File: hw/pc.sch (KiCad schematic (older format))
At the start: 10 parts

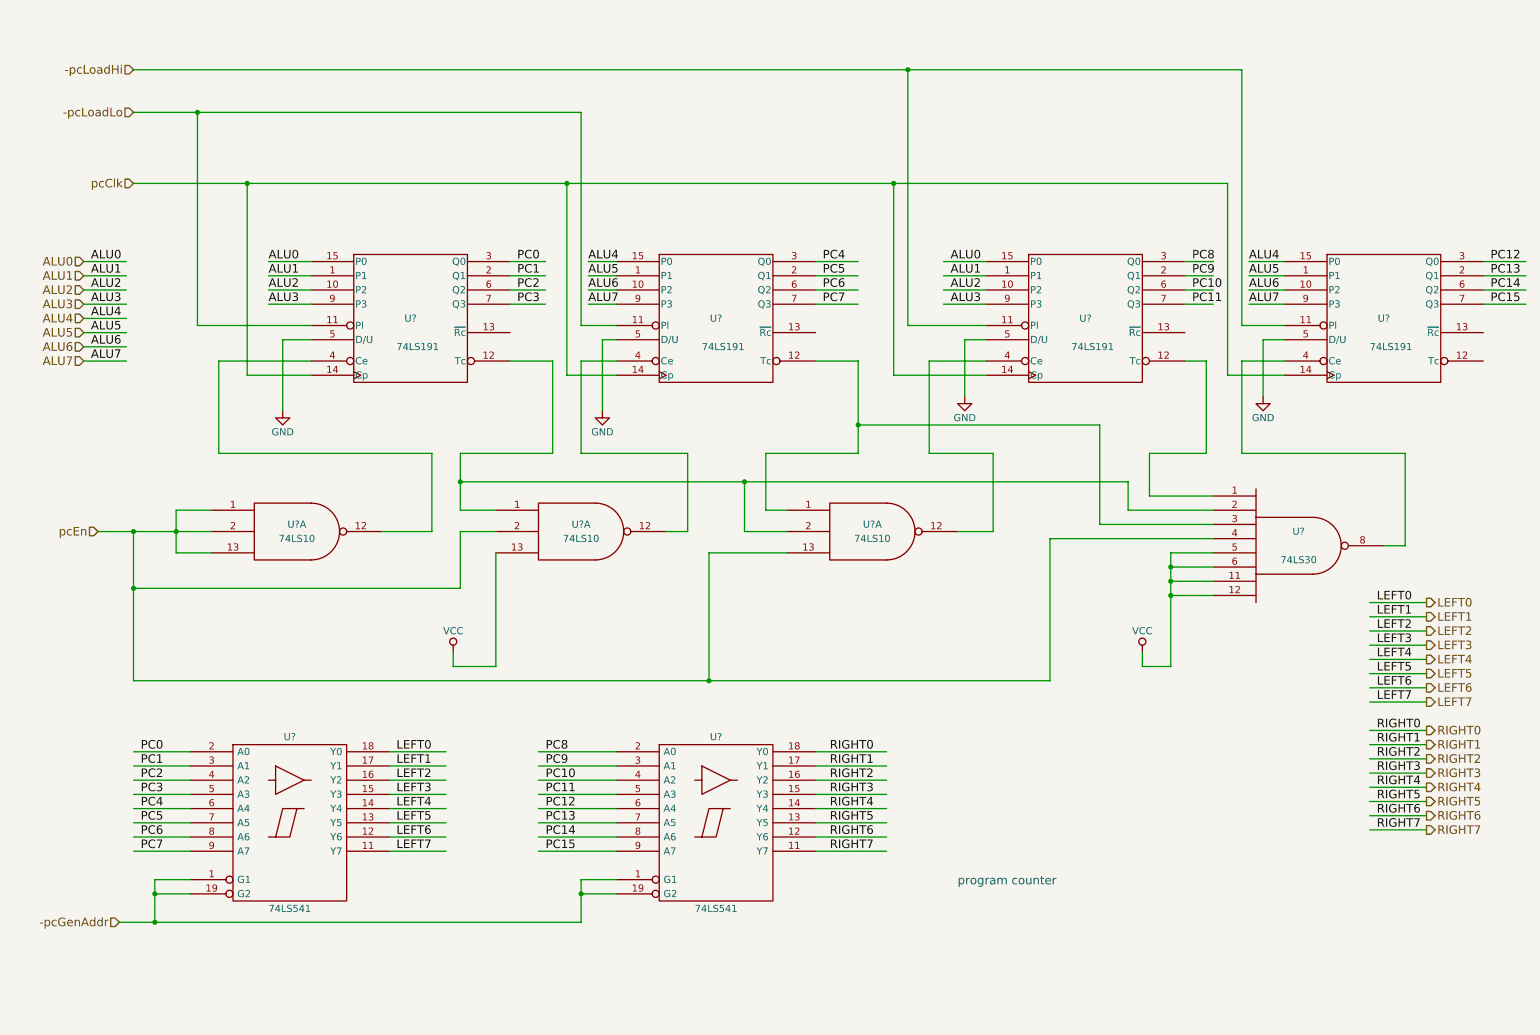
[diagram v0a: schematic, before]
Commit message: annotated more components
Also some more work on connecting modules together
and adding glue logic.
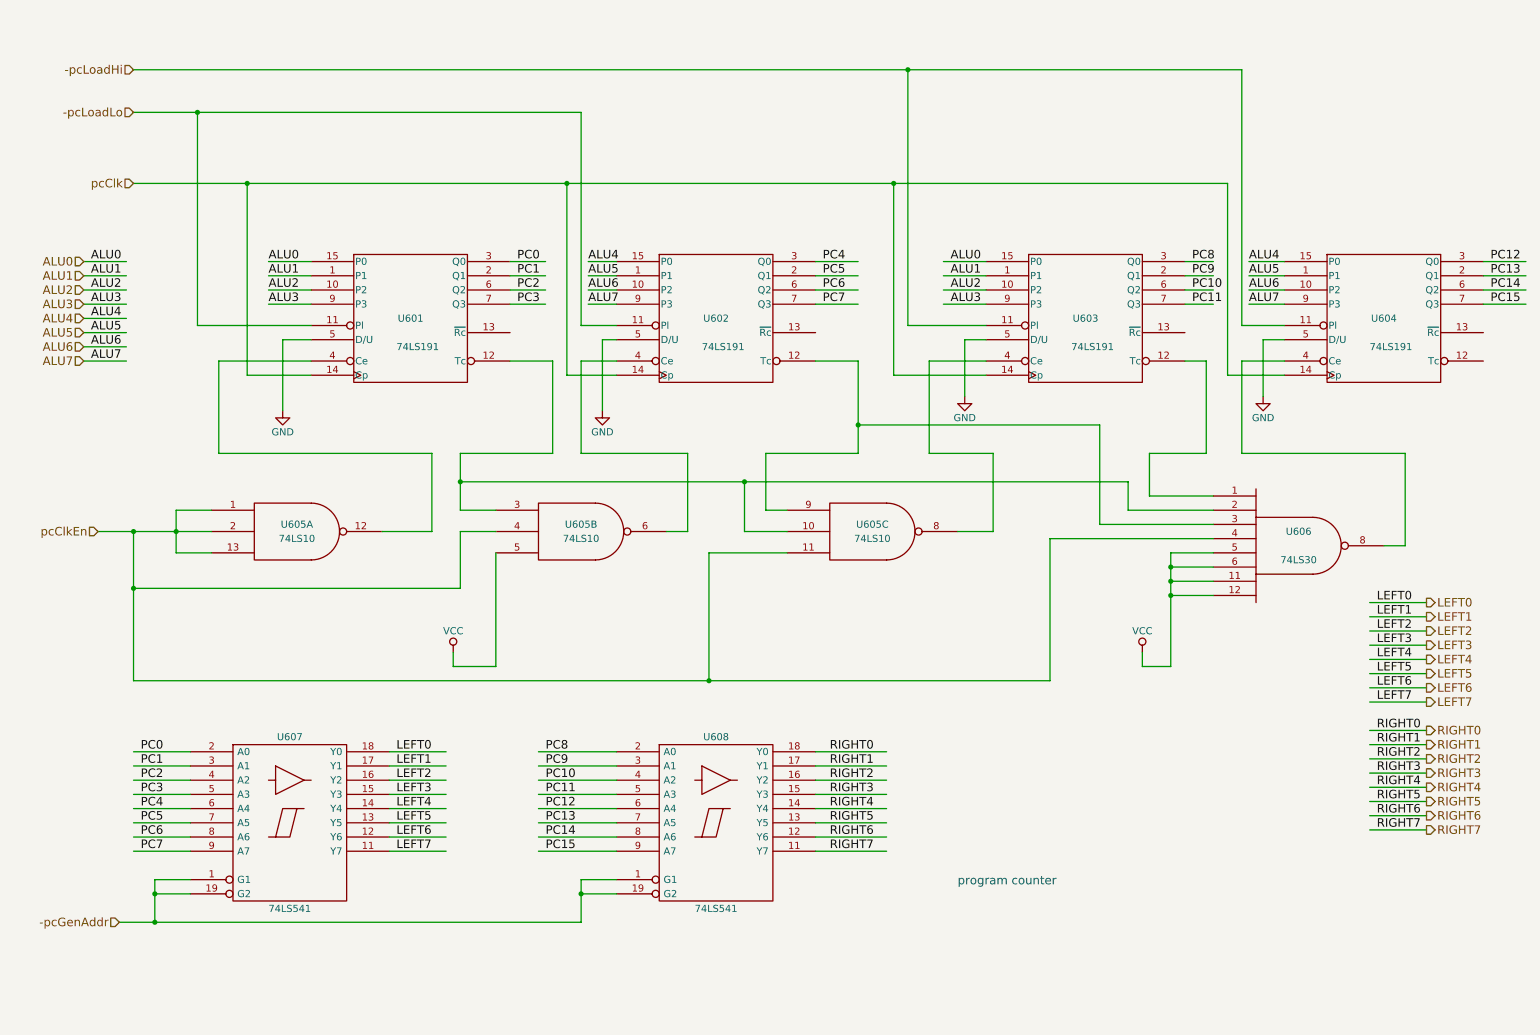
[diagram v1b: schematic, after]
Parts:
- gave numbers to parts that had none: 8
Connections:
- net labels added: pcClkEn
- net labels removed: pcEn
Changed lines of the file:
@@
 $EndDescr
 $Comp
-L 74LS10 U?
+L 74LS10 U605
 U 1 1 592B9492
 P 2500 4250
-F 0 "U?" H 2500 4300 50  0000 C CNN
+F 0 "U605" H 2500 4300 50  0000 C CNN
 F 1 "74LS10" H 2500 4200 50  0000 C CNN
 F 2 "" H 2500 4250 50  0001 C CNN
@@
 $EndComp
 $Comp
-L 74LS30 U?
+L 74LS30 U606
 U 1 1 592B9499
 P 9550 4350
-F 0 "U?" H 9550 4450 50  0000 C CNN
+F 0 "U606" H 9550 4450 50  0000 C CNN
 F 1 "74LS30" H 9550 4250 50  0000 C CNN
 F 2 "" H 9550 4350 50  0001 C CNN
@@
 $EndComp
 $Comp
-L 74LS191 U?
+L 74LS191 U601
 U 1 1 592B94A0
 P 3300 2750
-F 0 "U?" H 3300 2750 50  0000 C CNN
+F 0 "U601" H 3300 2750 50  0000 C CNN
 F 1 "74LS191" H 3350 2550 50  0000 C CNN
 F 2 "" H 3300 2750 50  0001 C CNN
@@
 $EndComp
 $Comp
-L 74LS191 U?
+L 74LS191 U602
 U 1 1 592B94A7
 P 5450 2750
-F 0 "U?" H 5450 2750 50  0000 C CNN
+F 0 "U602" H 5450 2750 50  0000 C CNN
 F 1 "74LS191" H 5500 2550 50  0000 C CNN
 F 2 "" H 5450 2750 50  0001 C CNN
@@
 $EndComp
 $Comp
-L 74LS191 U?
+L 74LS191 U603
 U 1 1 592B94AE
 P 8050 2750
-F 0 "U?" H 8050 2750 50  0000 C CNN
+F 0 "U603" H 8050 2750 50  0000 C CNN
 F 1 "74LS191" H 8100 2550 50  0000 C CNN
 F 2 "" H 8050 2750 50  0001 C CNN
@@
 $EndComp
 $Comp
-L 74LS191 U?
+L 74LS191 U604
 U 1 1 592B94B5
 P 10150 2750
-F 0 "U?" H 10150 2750 50  0000 C CNN
+F 0 "U604" H 10150 2750 50  0000 C CNN
 F 1 "74LS191" H 10200 2550 50  0000 C CNN
 F 2 "" H 10150 2750 50  0001 C CNN
@@
 $EndComp
 $Comp
-L 74LS10 U?
-U 1 1 592B94BC
+L 74LS10 U605
+U 2 1 592B94BC
 P 4500 4250
-F 0 "U?" H 4500 4300 50  0000 C CNN
+F 0 "U605" H 4500 4300 50  0000 C CNN
 F 1 "74LS10" H 4500 4200 50  0000 C CNN
 F 2 "" H 4500 4250 50  0001 C CNN
 F 3 "" H 4500 4250 50  0001 C CNN
-	1    4500 4250
-	1    0    0    -1
-$EndComp
-$Comp
-L 74LS10 U?
-U 1 1 592B94C3
+	2    4500 4250
+	1    0    0    -1
+$EndComp
+$Comp
+L 74LS10 U605
+U 3 1 592B94C3
 P 6550 4250
-F 0 "U?" H 6550 4300 50  0000 C CNN
+F 0 "U605" H 6550 4300 50  0000 C CNN
 F 1 "74LS10" H 6550 4200 50  0000 C CNN
 F 2 "" H 6550 4250 50  0001 C CNN
 F 3 "" H 6550 4250 50  0001 C CNN
-	1    6550 4250
+	3    6550 4250
 	1    0    0    -1
 $EndComp
@@
 $EndComp
 $Comp
-L 74LS541 U?
+L 74LS541 U607
 U 1 1 592B94F7
 P 2450 6300
-F 0 "U?" H 2450 6875 50  0000 C BNN
+F 0 "U607" H 2450 6875 50  0000 C BNN
 F 1 "74LS541" H 2450 5725 50  0000 C TNN
 F 2 "" H 2450 6300 50  0001 C CNN
@@
 $EndComp
 $Comp
-L 74LS541 U?
+L 74LS541 U608
 U 1 1 592B94FE
 P 5450 6300
-F 0 "U?" H 5450 6875 50  0000 C BNN
+F 0 "U608" H 5450 6875 50  0000 C BNN
 F 1 "74LS541" H 5450 5725 50  0000 C TNN
 F 2 "" H 5450 6300 50  0001 C CNN
@@
 pcClk
 Text HLabel 1100 4250 0    60   Input ~ 0
-pcEn
+pcClkEn
 Text HLabel 1250 7000 0    60   Input ~ 0
 -pcGenAddr

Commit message: eliminated pcClkEn signal
There's no need to selectively enable/disable
the count function in the PC because the PC
clock signal (pcClk) is generated explicitly
by the microcode, and clock pulses are sent
only when we actually want to increment the PC
value.

This allowed a simplicification of the carry
logic, and eliminated the need for the 74HC30
in the last stage of the carry logic.
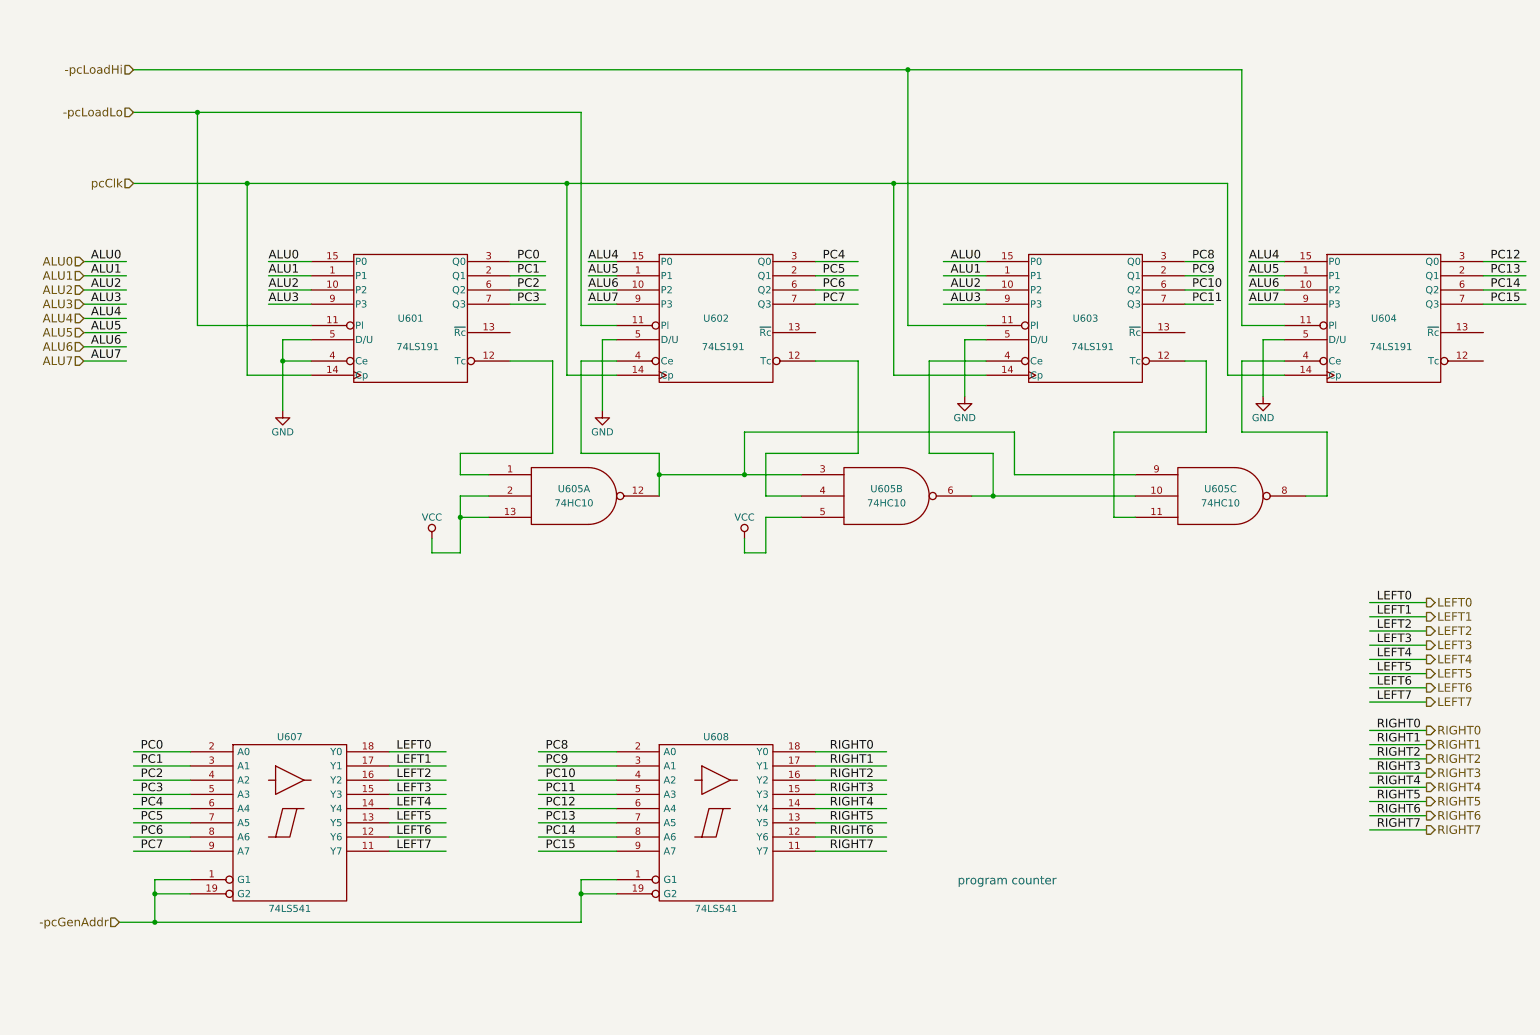
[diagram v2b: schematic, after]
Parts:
- removed U606: 74LS30, symbol 74LS30
- U605: value 74LS10 -> 74HC10
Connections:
- net labels removed: pcClkEn
- wire segments 188 -> 179

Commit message: fix PC carry logic
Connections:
- wire segments 179 -> 169
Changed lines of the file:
@@
 L GND #PWR?
 U 1 1 592B94E2
-P 4650 3400
-F 0 "#PWR?" H 4650 3150 50  0001 C CNN
-F 1 "GND" H 4650 3250 50  0000 C CNN
-F 2 "" H 4650 3400 50  0001 C CNN
-F 3 "" H 4650 3400 50  0001 C CNN
-	1    4650 3400
+P 4650 3250
+F 0 "#PWR?" H 4650 3000 50  0001 C CNN
+F 1 "GND" H 4650 3100 50  0000 C CNN
+F 2 "" H 4650 3250 50  0001 C CNN
+F 3 "" H 4650 3250 50  0001 C CNN
+	1    4650 3250
 	1    0    0    -1
 $EndComp
@@
 L GND #PWR?
 U 1 1 592B94E8
-P 7200 3300
-F 0 "#PWR?" H 7200 3050 50  0001 C CNN
-F 1 "GND" H 7200 3150 50  0000 C CNN
-F 2 "" H 7200 3300 50  0001 C CNN
-F 3 "" H 7200 3300 50  0001 C CNN
-	1    7200 3300
+P 7200 3200
+F 0 "#PWR?" H 7200 2950 50  0001 C CNN
+F 1 "GND" H 7200 3050 50  0000 C CNN
+F 2 "" H 7200 3200 50  0001 C CNN
+F 3 "" H 7200 3200 50  0001 C CNN
+	1    7200 3200
 	1    0    0    -1
 $EndComp
@@
 	2600 2900 2400 2900
 Wire Wire Line
-	2400 2900 2400 3050
-Wire Wire Line
-	2400 3050 2400 3400
+	2400 2900 2400 3400
 Wire Wire Line
 	4750 2900 4650 2900
 Wire Wire Line
-	4650 2900 4650 3400
+	4650 2900 4650 3250
 Wire Wire Line
 	7350 2900 7200 2900
 Wire Wire Line
-	7200 2900 7200 3300
+	7200 2900 7200 3200
 Wire Wire Line
 	9450 2900 9300 2900
@@
 	9450 3150 9050 3150
 Wire Wire Line
-	9050 3150 9050 1800
-Wire Wire Line
-	9050 1800 6700 1800
-Wire Wire Line
-	6700 1800 4400 1800
-Wire Wire Line
-	4400 1800 2150 1800
-Wire Wire Line
-	2150 1800 1350 1800
+	9050 1800 9050 3150
+Wire Wire Line
+	1350 1800 9050 1800
 Wire Wire Line
 	7350 3150 6700 3150
@@
 	1800 2800 1800 1300
 Wire Wire Line
-	1350 1300 1800 1300
-Wire Wire Line
-	1800 1300 4500 1300
+	1350 1300 4500 1300
 Wire Wire Line
 	4750 2800 4500 2800
@@
 	6800 2800 6800 1000
 Wire Wire Line
-	1350 1000 6800 1000
-Wire Wire Line
-	6800 1000 9150 1000
+	1350 1000 9150 1000
 Wire Wire Line
 	9450 2800 9150 2800
@@
 	1750 6700 1500 6700
 Wire Wire Line
-	1500 6700 1500 6800
-Wire Wire Line
-	1500 6800 1500 7000
+	1500 6700 1500 7000
 Wire Wire Line
 	1750 6800 1500 6800
 Connection ~ 1500 6800
 Wire Wire Line
-	4500 7000 1500 7000
-Wire Wire Line
-	1500 7000 1250 7000
+	4500 7000 1250 7000
 Wire Wire Line
 	4750 6700 4500 6700
 Wire Wire Line
-	4500 6700 4500 6800
-Wire Wire Line
-	4500 6800 4500 7000
+	4500 6700 4500 7000
 Connection ~ 1500 7000
 Wire Wire Line
@@
 	4300 3700 3650 3700
 Wire Wire Line
-	5050 4000 5050 3850
-Wire Wire Line
-	5050 3850 5050 3700
+	5050 3700 5050 4000
 Wire Wire Line
 	5050 3700 4500 3700
@@
 	4500 3700 4500 3050
 Wire Wire Line
-	6050 3850 5650 3850
-Wire Wire Line
-	5650 3850 5050 3850
-Connection ~ 5050 3850
-Wire Wire Line
 	6450 3050 6450 3700
 Wire Wire Line
@@
 	5650 4400 5650 4300
 Wire Wire Line
-	7250 4000 7400 4000
-Wire Wire Line
-	7400 4000 8400 4000
-Wire Wire Line
 	7400 4000 7400 3700
 Wire Wire Line
@@
 	8400 3850 7550 3850
 Wire Wire Line
-	7550 3850 7550 3550
-Wire Wire Line
-	7550 3550 5650 3550
-Wire Wire Line
-	5650 3550 5650 3850
-Connection ~ 5650 3850
-Connection ~ 7400 4000
+	7550 3550 7550 3850
+Wire Wire Line
+	4300 3550 7550 3550
 Wire Wire Line
 	8900 3050 8900 3550
@@
 	3850 4150 3650 4150
 Wire Wire Line
-	3650 4000 3650 4150
-Wire Wire Line
-	3650 4150 3650 4400
+	3650 4000 3650 4400
 Wire Wire Line
 	3650 4400 3450 4400
@@
 	1    0    0    -1
 $EndComp
+Connection ~ 4300 3550
+Wire Wire Line
+	6050 3850 5150 3850
+Wire Wire Line
+	5150 3850 5150 3550
+Connection ~ 5150 3550
+Wire Wire Line
+	7400 4000 7250 4000
+Wire Wire Line
+	8400 4000 7700 4000
+Wire Wire Line
+	7700 4000 7700 3450
+Wire Wire Line
+	7700 3450 6450 3450
+Connection ~ 6450 3450
 $EndSCHEMATC

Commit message: moved PC glue logic to PC schematic
I think it would be best to keep all of the logic
to the individual schematics, rather than putting
any in the main schematic.  More modular that way.
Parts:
- added U606: 74HC00, symbol 74LS00
- U601, U602, U603, U604: value 74LS191 -> 74HC191
- U607, U608: value 74LS541 -> 74HC541
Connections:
- net labels added: -uWrPCHi, -uWrPCLo, -wrPC, opIncPC, uPcClk
- wire segments 169 -> 187
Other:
- moved on the sheet: U601, U602, U603, U604, U605A, U605B, U605C, U607, U608
